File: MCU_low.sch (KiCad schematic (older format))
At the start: 105 parts, among them J10 Nucleo_SWD, J9 STLinkV2, Q15 BSS138, Q16 BSS138, SW10 ESC, SW4 RST, SW5 Encoder, SW6 X, SW7 UP, SW8 DOWN, SW9 ENTER, U25 LCD_I2C, U26 STM32L431RBTx, U27 ADS131M06, Y1 8.192, Y2 32.768, Y3 8.192

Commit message: - PCB WiP - Pump output aligned
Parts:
- R128, R129, R130, R131, R132, R133, R134, R135, R136, R137, R138, R139, R140, R141, R142, R143, R144, R145, R146, R147, R148, R149, R150, R151, R152, R153, R154, R155, R156, R157, R158, R159, R160, R161, R162: footprint Resistor_SMD:R_0603_1608Metric_Pad1.05x0.95mm_HandSolder -> Resistor_SMD:R_0603_1608Metric

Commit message: - PCB WiP
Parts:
- D23: footprint Diode_SMD:D_SOD-323 -> miscellaneous_my:D_SOD-323-523_HandSoldering
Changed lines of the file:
@@
 F 0 "D23" V 1100 2700 50  0000 R CNN
 F 1 "1N4448WS" V 1200 2700 50  0000 R CNN
-F 2 "Diode_SMD:D_SOD-323" H 1150 2625 50  0001 C CNN
+F 2 "miscellaneous_my:D_SOD-323-523_HandSoldering" H 1150 2625 50  0001 C CNN
 F 3 "https://www.vishay.com/docs/81387/1n4448ws.pdf" H 1150 2800 50  0001 C CNN
 	1    1150 2800

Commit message: - PCB WiP
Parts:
- removed C141: 10n, Capacitor_SMD:C_0603_1608Metric, symbol Device:C_Small
- removed R149, R155: 10k, Resistor_SMD:R_0603_1608Metric, symbol Device:R_Small
- removed SW6: X, Button_Switch_SMD:SW_Push_1P1T_NO_6x6mm_H9.5mm, symbol Switch:SW_Push
- removed TP27: TestPoint, TestPoint:TestPoint_THTPad_D1.5mm_Drill0.7mm, symbol Connector:TestPoint
- added L16, L17, L18, L19, L20, L21: BLM18TG102, Inductor_SMD:L_0603_1608Metric, symbol Device:L_Core_Ferrite_Small
- Y2: footprint Crystal:Crystal_AT310_D3.0mm_L10.0mm_Horizontal_1EP_style2 -> Crystal:Crystal_C38-LF_D3.0mm_L8.0mm_Horizontal_1EP_style1; symbol Device:Crystal_Small -> Device:Crystal_GND3_Small
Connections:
- net ADC_CS: now also L21.1; no longer U27.17 (~CS)
- net ADC_DRDY: now also L20.2; no longer U27.18 (~DRDY)
- net ADC_MISO: now also L18.2; no longer U27.20 (DOUT)
- net ADC_MOSI: now also L17.2; no longer U27.21 (DIN)
- net ADC_RESET: now also L16.2; no longer U27.16 (~SYNC~/~RESET)
- net ADC_SCK: now also L19.2; no longer U27.19 (SCLK)
- net GND: now also C133.2, D24.1 (K), D25.1 (K), D26.1 (K), D27.1 (K), Y2.3; no longer C133.1, R139.2, R140.2, R141.2, R142.2
- net LED_BLU: now also R142.1; no longer D27.2 (A)
- net LED_GRN: now also R139.1; no longer D24.2 (A)
- net LED_ORG: now also R140.1; no longer D25.2 (A)
- net LED_RED: now also R141.1; no longer D26.2 (A)
- net at C134.2, U26.4 (PC15): now also Y2.1; no longer Y2.2
- net KEY_5: no longer names the net of U26.36 (PB15)
- net KEY_DOWN renamed KEY_RIGHT
- net KEY_UP renamed KEY_LEFT
- new net: D24.2 (A), R139.2
- new net: C133.1, U26.3 (PC14), Y2.2
- new net: L16.1, U27.16 (~SYNC~/~RESET)
- new net: L21.2, U27.17 (~CS)
- new net: L20.1, U27.18 (~DRDY)
- new net: L19.1, U27.19 (SCLK)
- new net: L18.1, U27.20 (DOUT)
- new net: L17.1, U27.21 (DIN)
- new net: D25.2 (A), R140.2
- new net: D26.2 (A), R141.2
- new net: D27.2 (A), R142.2
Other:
- moved on the sheet: D24, D25, D26, D27, R139, R140, R141, R142

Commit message: - PCB WiP
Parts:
- added J13, J14: Conn_02x09_Odd_Even, Connector_PinSocket_2.54mm:PinSocket_2x09_P2.54mm_Vertical, symbol Connector_Generic:Conn_02x09_Odd_Even
- added TP27, TP39: TestPoint, TestPoint:TestPoint_THTPad_D1.5mm_Drill0.7mm, symbol Connector:TestPoint
- U25: footprint miscellaneous_my:HD44780_20x4_wPCF8574 -> Connector_PinHeader_2.54mm:PinHeader_1x04_P2.54mm_Vertical
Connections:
- net +3V3: now also J13.15 (Pin_15), J14.16 (Pin_16)
- net +5V: now also J13.13 (Pin_13), J14.14 (Pin_14)
- net +BATT: now also J13.9 (Pin_9), J14.10 (Pin_10)
- net ADC_CH0: now also TP27.1
- net ADC_CH1: now also TP39.1
- net ENC_A: now also J13.14 (Pin_14), J14.13 (Pin_13)
- net ENC_B: now also J13.16 (Pin_16), J14.15 (Pin_15)
- net ENC_SW: now also J13.12 (Pin_12), J14.11 (Pin_11)
- net GND: now also J13.1 (Pin_1), J13.17 (Pin_17), J13.7 (Pin_7), J14.18 (Pin_18), J14.2 (Pin_2), J14.8 (Pin_8)
- net KEY_ENTER: now also J13.6 (Pin_6), J14.5 (Pin_5)
- net KEY_ESC: now also J13.8 (Pin_8), J14.7 (Pin_7)
- net KEY_LEFT: now also J13.2 (Pin_2), J14.1 (Pin_1)
- net KEY_PWR: now also J13.10 (Pin_10), J14.9 (Pin_9)
- net KEY_RIGHT: now also J13.4 (Pin_4), J14.3 (Pin_3)
- net PWR_LOCK: now also J13.18 (Pin_18), J14.17 (Pin_17)
- net UART_RX: now also J13.5 (Pin_5), J14.6 (Pin_6)
- net UART_TX: now also J13.3 (Pin_3), J14.4 (Pin_4)
- new net +15V: J13.11 (Pin_11), J14.12 (Pin_12)

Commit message: - PCB WiP
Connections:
- net ENC_A: now also R137.2, R144.1, SW5.A; no longer C127.2, R144.2, U26.26 (PB0)
- net ENC_B: now also J13.12 (Pin_12), J14.11 (Pin_11), R138.1, R145.1, SW5.B; no longer C128.2, J13.16 (Pin_16), J14.15 (Pin_15), R145.2, U26.27 (PB1)
- net ENC_SW: now also J13.10 (Pin_10), J14.9 (Pin_9), R134.2, R135.1, SW5.S2; no longer C125.2, J13.12 (Pin_12), J14.11 (Pin_11), R135.2, U26.28 (PB2)
- net KEY_ENTER: now also R152.2, R158.1, SW9.2; no longer C144.2, R158.2, U26.39 (PC8)
- net KEY_ESC: now also R153.2, R159.1, SW10.2; no longer C145.2, R159.2, U26.40 (PC9)
- net KEY_LEFT: now also R150.2, R156.1, SW7.2; no longer C142.2, R156.2, U26.37 (PC6)
- net KEY_PWR: now also J13.18 (Pin_18), J14.17 (Pin_17); no longer J13.10 (Pin_10), J14.9 (Pin_9)
- net KEY_RIGHT: now also R151.2, R157.1, SW8.2; no longer C143.2, R157.2, U26.38 (PC7)
- net PWR_LOCK: now also J13.16 (Pin_16), J14.15 (Pin_15); no longer J13.18 (Pin_18), J14.17 (Pin_17)
- new net ENC_A_F: C127.2, R144.2, U26.26 (PB0)
- new net ENC_B_F: C128.2, R145.2, U26.27 (PB1)
- new net ENC_SW_F: C125.2, R135.2, U26.28 (PB2)
- new net ENTER: C144.2, R158.2, U26.39 (PC8)
- new net ESC: C145.2, R159.2, U26.40 (PC9)
- new net LEFT: C142.2, R156.2, U26.37 (PC6)
- new net RIGHT: C143.2, R157.2, U26.38 (PC7)
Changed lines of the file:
@@
 	10200 2400 10200 2450
 Text Label 10300 2400 0    50   ~ 0
-ENC_SW
+ENC_SW_F
 Text Label 9000 3400 0    50   ~ 0
-ENC_A
+ENC_A_F
 Text Label 9900 3400 0    50   ~ 0
-ENC_B
+ENC_B_F
 Wire Wire Line
 	10200 2400 10300 2400
@@
 	10400 3000 10400 2950
 Text Label 7100 3100 0    50   ~ 0
-ENC_SW
+ENC_SW_F
 Text Label 7100 2900 0    50   ~ 0
-ENC_A
+ENC_A_F
 Text Label 7100 3000 0    50   ~ 0
-ENC_B
+ENC_B_F
 Wire Wire Line
 	7000 2900 7100 2900
@@
 $EndComp
 Text Label 10800 6050 0    50   ~ 0
-KEY_ESC
+ESC
 Text Label 9850 6050 0    50   ~ 0
-KEY_ENTER
+ENTER
 $Comp
 L power:GND #PWR?
@@
 $EndComp
 Text Label 7950 6050 0    50   ~ 0
-KEY_LEFT
+LEFT
 $Comp
 L power:GND #PWR?
@@
 	7900 5700 7650 5700
 Text Label 8900 6050 0    50   ~ 0
-KEY_RIGHT
+RIGHT
 Text Label 5250 3800 0    50   ~ 0
-KEY_ESC
+ESC
 Text Label 5250 3700 0    50   ~ 0
-KEY_ENTER
+ENTER
 Text Label 5250 3600 0    50   ~ 0
-KEY_RIGHT
+RIGHT
 Text Label 5250 3500 0    50   ~ 0
-KEY_LEFT
+LEFT
 Wire Wire Line
 	5250 3500 5700 3500
@@
 Text Label 7050 4300 0    50   ~ 0
 KEY_PWR
+Text Label 9200 5050 0    50   ~ 0
+KEY_PWR
 Text Label 9200 4650 0    50   ~ 0
-KEY_PWR
-Text Label 9200 4750 0    50   ~ 0
 ENC_SW
 Text Label 9200 4850 0    50   ~ 0
 ENC_A
-Text Label 9200 4950 0    50   ~ 0
+Text Label 9200 4750 0    50   ~ 0
 ENC_B
 $Comp
@@
 Wire Wire Line
 	7000 2400 7500 2400
-Text Label 9200 5050 0    50   ~ 0
+Text Label 9200 4950 0    50   ~ 0
 PWR_LOCK
 Wire Wire Line
@@
 Text Label 10750 4250 0    50   ~ 0
 KEY_LEFT
+Text Label 10750 5050 0    50   ~ 0
+KEY_PWR
 Text Label 10750 4650 0    50   ~ 0
-KEY_PWR
-Text Label 10750 4750 0    50   ~ 0
 ENC_SW
 Text Label 10750 4850 0    50   ~ 0
 ENC_A
-Text Label 10750 4950 0    50   ~ 0
+Text Label 10750 4750 0    50   ~ 0
 ENC_B
 $Comp
@@
 Text Label 10250 4450 2    50   ~ 0
 UART_RX
-Text Label 10750 5050 0    50   ~ 0
+Text Label 10750 4950 0    50   ~ 0
 PWR_LOCK
 Wire Wire Line
@@
 	0    1    1    0
 $EndComp
+Text Label 10600 5700 0    50   ~ 0
+KEY_ESC
+Text Label 9650 5700 0    50   ~ 0
+KEY_ENTER
+Text Label 8700 5700 0    50   ~ 0
+KEY_RIGHT
+Text Label 7750 5700 0    50   ~ 0
+KEY_LEFT
+Text Label 9100 3000 0    50   ~ 0
+ENC_A
+Text Label 9800 3000 0    50   ~ 0
+ENC_B
+Text Label 9650 2400 0    50   ~ 0
+ENC_SW
 $EndSCHEMATC

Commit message: - PCB WiP
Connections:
- net +BATT: now also J13.17 (Pin_17), J14.18 (Pin_18); no longer J13.9 (Pin_9), J14.10 (Pin_10)
- net GND: now also J13.9 (Pin_9), J14.10 (Pin_10); no longer J13.17 (Pin_17), J14.18 (Pin_18)
- net KEY_ENTER: now also J13.4 (Pin_4), J14.3 (Pin_3); no longer J13.6 (Pin_6), J14.5 (Pin_5)
- net KEY_ESC: now also J13.2 (Pin_2), J14.1 (Pin_1); no longer J13.8 (Pin_8), J14.7 (Pin_7)
- net KEY_LEFT: now also J13.8 (Pin_8), J14.7 (Pin_7); no longer J13.2 (Pin_2), J14.1 (Pin_1)
- net KEY_RIGHT: now also J13.6 (Pin_6), J14.5 (Pin_5); no longer J13.4 (Pin_4), J14.3 (Pin_3)
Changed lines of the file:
@@
 	1    0    0    -1
 $EndComp
-Text Label 9200 4550 0    50   ~ 0
-KEY_ESC
-Text Label 9200 4450 0    50   ~ 0
-KEY_ENTER
-Text Label 9200 4350 0    50   ~ 0
-KEY_RIGHT
-Text Label 9200 4250 0    50   ~ 0
-KEY_LEFT
 Text Label 7050 4300 0    50   ~ 0
 KEY_PWR
@@
 L power:GND #PWR?
 U 1 1 5FC4B228
-P 8700 5050
+P 8700 4650
 AR Path="/5F40DCB9/5FC4B228" Ref="#PWR?"  Part="1"
 AR Path="/5F618AB9/5FC4B228" Ref="#PWR?"  Part="1"
@@
 AR Path="/5F620813/5FC4B228" Ref="#PWR?"  Part="1"
 AR Path="/5F7D6767/5FC4B228" Ref="#PWR0258"  Part="1"
-F 0 "#PWR0258" H 8700 4890 50  0001 C CNN
-F 1 "GND" H 8700 4950 39  0000 C TNN
-F 2 "" H 8700 5050 50  0001 C CNN
-F 3 "" H 8700 5050 50  0001 C CNN
-	1    8700 5050
-	1    0    0    -1
+F 0 "#PWR0258" H 8700 4490 50  0001 C CNN
+F 1 "GND" H 8700 4550 39  0000 C TNN
+F 2 "" H 8700 4650 50  0001 C CNN
+F 3 "" H 8700 4650 50  0001 C CNN
+	1    8700 4650
+	0    1    1    0
 $EndComp
 $Comp
@@
 L power:+BATT #PWR?
 U 1 1 5FC4CF35
-P 8700 4650
+P 8700 5050
 AR Path="/5F620813/5FC4CF35" Ref="#PWR?"  Part="1"
 AR Path="/5F7A93EE/5FC4CF35" Ref="#PWR?"  Part="1"
 AR Path="/5F7D6767/5FC4CF35" Ref="#PWR0182"  Part="1"
-F 0 "#PWR0182" H 8700 4500 50  0001 C CNN
-F 1 "+BATT" V 8700 4900 50  0000 C CNN
-F 2 "" H 8700 4650 50  0001 C CNN
-F 3 "" H 8700 4650 50  0001 C CNN
-	1    8700 4650
+F 0 "#PWR0182" H 8700 4900 50  0001 C CNN
+F 1 "+BATT" V 8700 5300 50  0000 C CNN
+F 2 "" H 8700 5050 50  0001 C CNN
+F 3 "" H 8700 5050 50  0001 C CNN
+	1    8700 5050
 	0    -1   -1   0
 $EndComp
@@
 	-1   0    0    -1
 $EndComp
+Text Label 10750 4250 0    50   ~ 0
+KEY_ESC
+Text Label 10750 4350 0    50   ~ 0
+KEY_ENTER
+Text Label 10750 4450 0    50   ~ 0
+KEY_RIGHT
 Text Label 10750 4550 0    50   ~ 0
-KEY_ESC
-Text Label 10750 4450 0    50   ~ 0
-KEY_ENTER
-Text Label 10750 4350 0    50   ~ 0
-KEY_RIGHT
-Text Label 10750 4250 0    50   ~ 0
 KEY_LEFT
 Text Label 10750 5050 0    50   ~ 0
@@
 L power:GND #PWR?
 U 1 1 5FD7FD79
-P 10250 5050
+P 10250 4650
 AR Path="/5F40DCB9/5FD7FD79" Ref="#PWR?"  Part="1"
 AR Path="/5F618AB9/5FD7FD79" Ref="#PWR?"  Part="1"
@@
 AR Path="/5F620813/5FD7FD79" Ref="#PWR?"  Part="1"
 AR Path="/5F7D6767/5FD7FD79" Ref="#PWR0259"  Part="1"
-F 0 "#PWR0259" H 10250 4890 50  0001 C CNN
-F 1 "GND" H 10250 4950 39  0000 C TNN
-F 2 "" H 10250 5050 50  0001 C CNN
-F 3 "" H 10250 5050 50  0001 C CNN
-	1    10250 5050
-	1    0    0    -1
+F 0 "#PWR0259" H 10250 4490 50  0001 C CNN
+F 1 "GND" H 10250 4550 39  0000 C TNN
+F 2 "" H 10250 4650 50  0001 C CNN
+F 3 "" H 10250 4650 50  0001 C CNN
+	1    10250 4650
+	0    1    1    0
 $EndComp
 $Comp
@@
 L power:+BATT #PWR?
 U 1 1 5FD7FD8B
-P 10250 4650
+P 10250 5050
 AR Path="/5F620813/5FD7FD8B" Ref="#PWR?"  Part="1"
 AR Path="/5F7A93EE/5FD7FD8B" Ref="#PWR?"  Part="1"
 AR Path="/5F7D6767/5FD7FD8B" Ref="#PWR0251"  Part="1"
-F 0 "#PWR0251" H 10250 4500 50  0001 C CNN
-F 1 "+BATT" V 10250 4900 50  0000 C CNN
-F 2 "" H 10250 4650 50  0001 C CNN
-F 3 "" H 10250 4650 50  0001 C CNN
-	1    10250 4650
+F 0 "#PWR0251" H 10250 4900 50  0001 C CNN
+F 1 "+BATT" V 10250 5300 50  0000 C CNN
+F 2 "" H 10250 5050 50  0001 C CNN
+F 3 "" H 10250 5050 50  0001 C CNN
+	1    10250 5050
 	0    -1   -1   0
 $EndComp
@@
 Text Label 9650 2400 0    50   ~ 0
 ENC_SW
+Text Label 9200 4250 0    50   ~ 0
+KEY_ESC
+Text Label 9200 4350 0    50   ~ 0
+KEY_ENTER
+Text Label 9200 4450 0    50   ~ 0
+KEY_RIGHT
+Text Label 9200 4550 0    50   ~ 0
+KEY_LEFT
 $EndSCHEMATC

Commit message: - PCB WiP
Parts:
- removed J13, J14: Conn_02x09_Odd_Even, Connector_PinSocket_2.54mm:PinSocket_2x09_P2.54mm_Vertical, symbol Connector_Generic:Conn_02x09_Odd_Even
- added J13, J14: Conn_02x10_Odd_Even, Connector_PinSocket_2.54mm:PinSocket_2x10_P2.54mm_Vertical, symbol Connector_Generic:Conn_02x10_Odd_Even
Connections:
- net +15V: now also J13.3 (Pin_3), J14.4 (Pin_4)
- net +3V3: now also J13.17 (Pin_17), J14.18 (Pin_18)
- net +5V: now also J13.15 (Pin_15), J14.16 (Pin_16)
- net +BATT: now also J13.19 (Pin_19), J14.20 (Pin_20)
- net ENC_A: now also J13.16 (Pin_16), J14.15 (Pin_15)
- net ENC_B: now also J13.14 (Pin_14), J14.13 (Pin_13)
- net ENC_SW: now also J13.12 (Pin_12), J14.11 (Pin_11)
- net GND: now also J13.11 (Pin_11), J13.13 (Pin_13), J13.4 (Pin_4), J14.12 (Pin_12), J14.14 (Pin_14), J14.3 (Pin_3)
- net KEY_ENTER: now also J13.8 (Pin_8), J14.7 (Pin_7)
- net KEY_ESC: now also J13.6 (Pin_6), J14.5 (Pin_5)
- net KEY_LEFT: now also J13.10 (Pin_10), J14.9 (Pin_9)
- net KEY_PWR: now also U26.36 (PB15), J13.20 (Pin_20), J14.19 (Pin_19); no longer U26.35 (PB14)
- net KEY_RIGHT: now also J13.9 (Pin_9), J14.10 (Pin_10)
- net PWR_LOCK: now also U26.35 (PB14), J13.18 (Pin_18), J14.17 (Pin_17); no longer U26.45 (PA12)
- net UART_RX: now also J13.7 (Pin_7), J14.8 (Pin_8)
- net UART_TX: now also J13.5 (Pin_5), J14.6 (Pin_6)
- new net +12V: J13.1 (Pin_1), J14.2 (Pin_2)
- new net -5V: J13.2 (Pin_2), J14.1 (Pin_1)

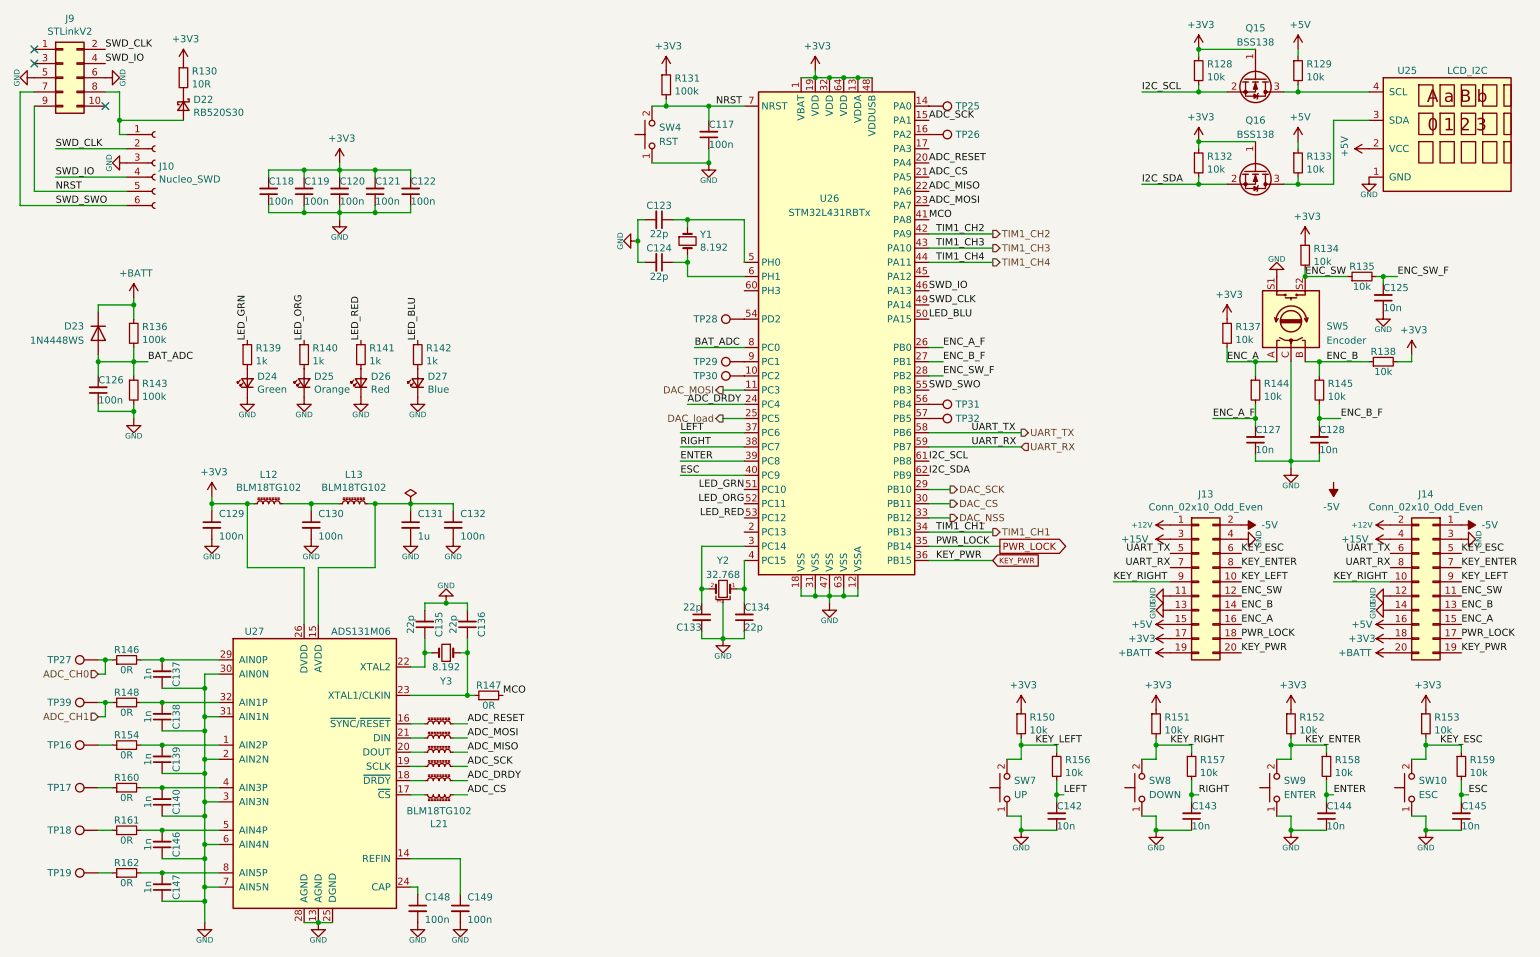
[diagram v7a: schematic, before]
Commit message: - as-built changes - add custom library elements
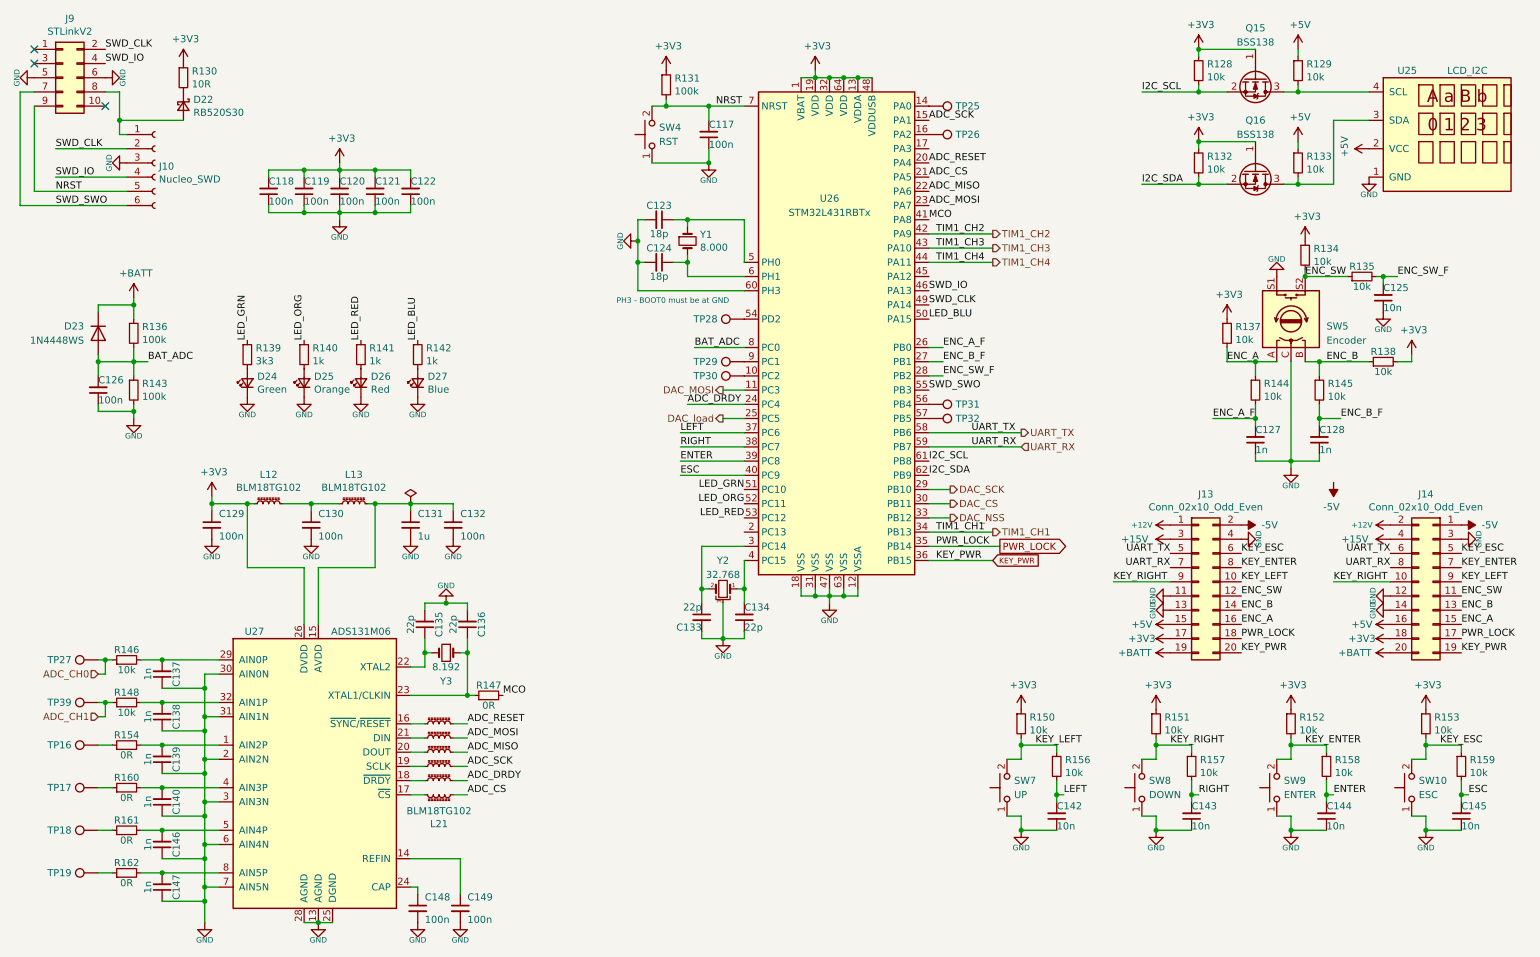
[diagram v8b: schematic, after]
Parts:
- C123, C124: value 22p -> 18p
- C127, C128: value 10n -> 1n
- R139: value 1k -> 3k3
- R146, R148: value 0R -> 10k
- Y1: value 8.192 -> 8.000
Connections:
- net GND: now also U26.60 (PH3)
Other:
- note added: "PH3 - BOOT0 must be at GND"
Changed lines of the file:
@@
 encoding utf-8
 Sheet 7 10
-Title ""
-Date ""
-Rev ""
-Comp ""
+Title "Procesor - anoda"
+Date "2021-01-18"
+Rev "1.0"
+Comp "Łukasz Sitarek"
 Comment1 ""
 Comment2 ""
@@
 P 2200 2950
 F 0 "R139" H 2259 2996 50  0000 L CNN
-F 1 "1k" H 2259 2905 50  0000 L CNN
+F 1 "3k3" H 2259 2905 50  0000 L CNN
 F 2 "Resistor_SMD:R_0603_1608Metric" H 2200 2950 50  0001 C CNN
 F 3 "~" H 2200 2950 50  0001 C CNN
@@
 P 5300 2150
 F 0 "Y1" V 5254 2238 50  0000 L CNN
-F 1 "8.192" V 5345 2238 50  0000 L CNN
+F 1 "8.000" V 5345 2238 50  0000 L CNN
 F 2 "Crystal:Crystal_HC49-4H_Vertical" H 5300 2150 50  0001 C CNN
 F 3 "~" H 5300 2150 50  0001 C CNN
@@
 AR Path="/5F61C123/5FC26E91" Ref="C?"  Part="1"
 F 0 "C123" V 5000 2000 50  0000 C CNN
-F 1 "22p" V 5200 2000 50  0000 C CNN
+F 1 "18p" V 5200 2000 50  0000 C CNN
 F 2 "Capacitor_SMD:C_0603_1608Metric" H 5100 2000 50  0001 C CNN
 F 3 "~" H 5100 2000 50  0001 C CNN
@@
 AR Path="/5F61C123/5FC28548" Ref="C?"  Part="1"
 F 0 "C124" V 5000 2300 50  0000 C CNN
-F 1 "22p" V 5200 2300 50  0000 C CNN
+F 1 "18p" V 5200 2300 50  0000 C CNN
 F 2 "Capacitor_SMD:C_0603_1608Metric" H 5100 2300 50  0001 C CNN
 F 3 "~" H 5100 2300 50  0001 C CNN
@@
 AR Path="/5F61C123/5FC9561D" Ref="C?"  Part="1"
 F 0 "C128" H 9750 3450 50  0000 R BNN
-F 1 "10n" H 9750 3650 50  0000 R TNN
+F 1 "1n" H 9750 3650 50  0000 R TNN
 F 2 "Capacitor_SMD:C_0603_1608Metric" H 9750 3550 50  0001 C CNN
 F 3 "~" H 9750 3550 50  0001 C CNN
@@
 AR Path="/5F61C123/5FC95887" Ref="C?"  Part="1"
 F 0 "C127" H 9300 3450 50  0000 R BNN
-F 1 "10n" H 9300 3650 50  0000 R TNN
+F 1 "1n" H 9300 3650 50  0000 R TNN
 F 2 "Capacitor_SMD:C_0603_1608Metric" H 9300 3550 50  0001 C CNN
 F 3 "~" H 9300 3550 50  0001 C CNN
@@
 AR Path="/5F7D6767/5FEEB6F5" Ref="R146"  Part="1"
 F 0 "R146" V 1450 5100 50  0000 C BNN
-F 1 "0R" V 1250 5100 50  0000 C TNN
+F 1 "10k" V 1250 5100 50  0000 C TNN
 F 2 "Resistor_SMD:R_0603_1608Metric" V 1280 5100 50  0001 C CNN
 F 3 "~" H 1350 5100 50  0001 C CNN
@@
 AR Path="/5F7D6767/5FF7A726" Ref="R148"  Part="1"
 F 0 "R148" V 1450 5400 50  0000 C BNN
-F 1 "0R" V 1250 5400 50  0000 C TNN
+F 1 "10k" V 1250 5400 50  0000 C TNN
 F 2 "Resistor_SMD:R_0603_1608Metric" V 1280 5400 50  0001 C CNN
 F 3 "~" H 1350 5400 50  0001 C CNN
@@
 	0    -1   -1   0
 $EndComp
+Wire Wire Line
+	5700 2500 4950 2500
+Wire Wire Line
+	4950 2500 4950 2300
+Connection ~ 4950 2300
+Text Notes 4800 2600 0    39   ~ 0
+PH3 - BOOT0 must be at GND
 $EndSCHEMATC
